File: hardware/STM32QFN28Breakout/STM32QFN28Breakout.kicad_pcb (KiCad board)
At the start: 2 copper layers, 22.7 x 34.6 mm, 21 parts, among them J5 Conn_01x11_Male, J6 Conn_01x11_Male, U1 STM32G031F4Px, U2 AP2112K-3.3, Y1 ECS-3225MVQ-160-BP-TR

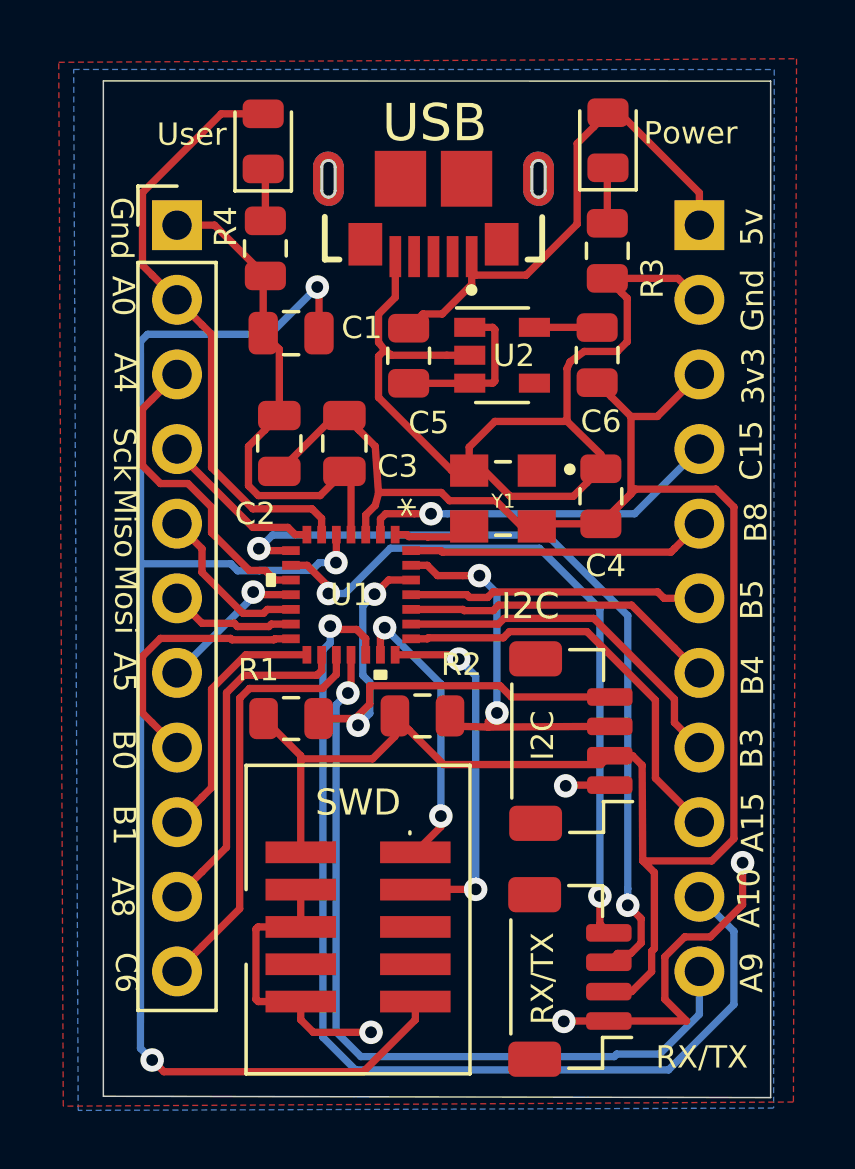
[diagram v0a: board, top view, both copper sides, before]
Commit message: fix and tweaks for STM32QFN28 breakout PCB
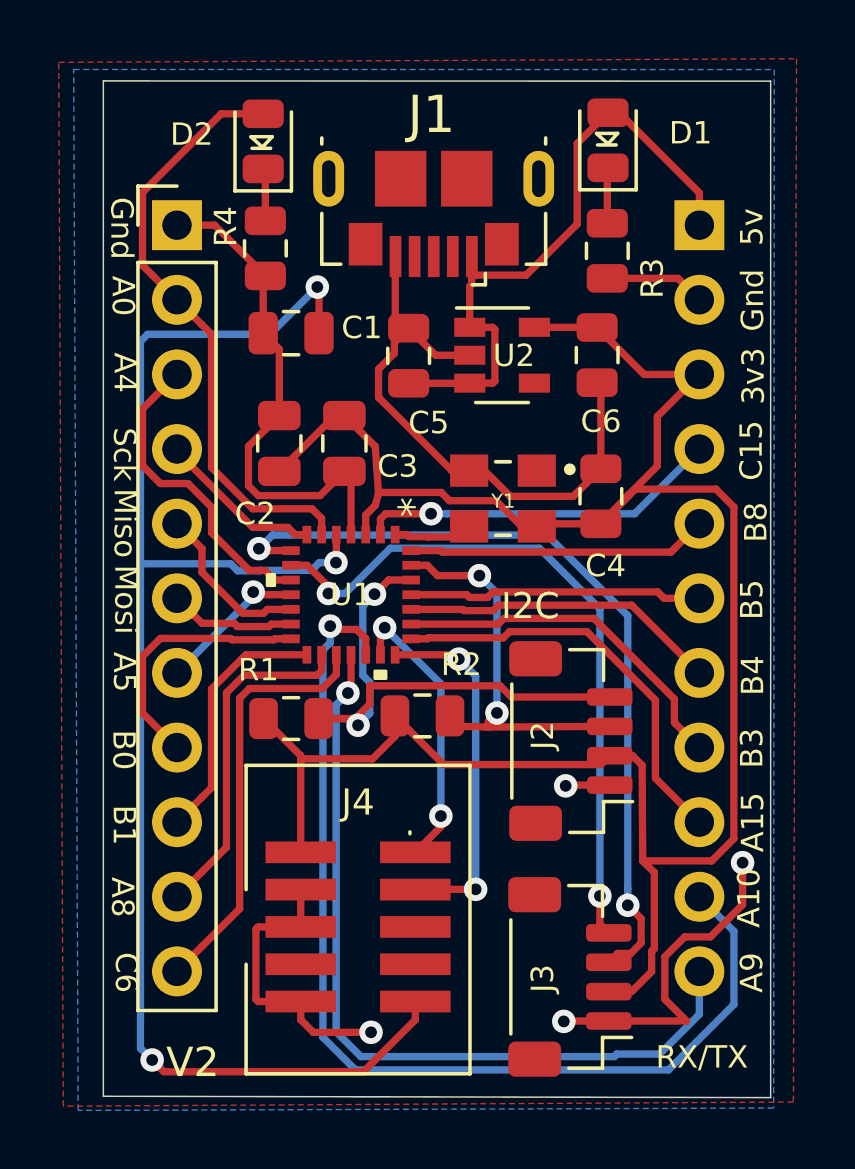
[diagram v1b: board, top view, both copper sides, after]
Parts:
- J1: renamed from USB; footprint Useful Modifications:GCT_USB3076-XX-X_REVC -> Useful Modifications:USB_Micro-B_GCT_USB3076-30-A
- moved J1 1.20 mm to (211.9, 80.9)
- renumbered Power to D1, User to D2, I2C to J2, RX/TX to J3, SWD to J4
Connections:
- C5 pad 1: Net-(C5-Pad1) -> +5V
- C5 pad 2: +5V -> GND
- C6 pad 1: +3V3 -> GND
- C6 pad 2: Net-(C6-Pad2) -> +3V3
- U2 pad 1: Net-(C5-Pad1) -> +5V
- U2 pad 3: Net-(C5-Pad1) -> +5V
- U2 pad 5: Net-(C6-Pad2) -> +3V3
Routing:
- net GND: track 74.8 -> 64.1 mm
- net Net-(C5-Pad1): track 5.60 -> 0.00 mm
- net +5V: track 18.1 -> 22.5 mm
- net +3V3: track 72.0 -> 76.2 mm
- net Net-(C6-Pad2): track 2.14 -> 0.00 mm
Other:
- board text added: "STM32G031G8U6 Breakout V2"
- board text added: "V2"

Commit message: updates to STM32QFN28 breakout moving to 0603 components
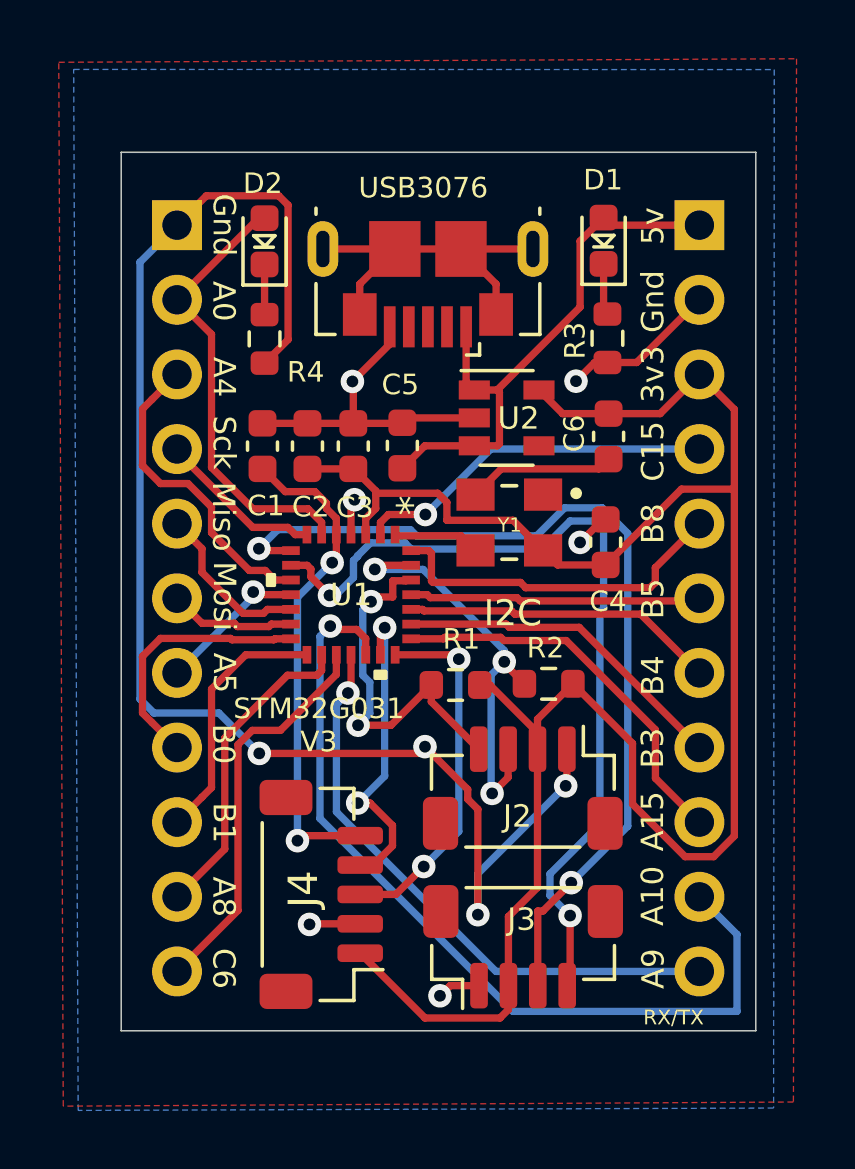
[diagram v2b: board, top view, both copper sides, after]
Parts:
- C1, C2, C3, C4, C5, C6: footprint Capacitor_SMD:C_0805_2012Metric -> Capacitor_SMD:C_0603_1608Metric
- D1, D2: footprint LED_SMD:LED_0805_2012Metric -> LED_SMD:LED_0603_1608Metric
- J1: value USB3076-XX-X_REVC -> USB3076
- J4: value Conn_ARM_JTAG_SWD_10 -> Conn_01x05_Male; footprint Useful Modifications:JTAG_SWD_SMD -> Connector_JST:JST_SH_BM05B-SRSS-TB_1x05-1MP_P1.00mm_Vertical
- R1, R2, R3, R4: footprint Resistor_SMD:R_0805_2012Metric -> Resistor_SMD:R_0603_1608Metric
- moved R1 5.71 mm to (212.7, 96.9), turned to 0 degrees
- moved R2 4.43 mm to (215.8, 96.9), turned to 0 degrees
- moved C1 3.97 mm to (206.1, 88.8), turned to 90 degrees
- moved D1 3.42 mm to (217.7, 81.8)
- moved D2 3.40 mm to (206.2, 81.8)
- moved R4 3.08 mm to (206.2, 85.2)
- moved C5 3.06 mm to (210.9, 88.8)
- moved R3 2.98 mm to (217.8, 85.1)
- moved C6 2.80 mm to (217.9, 88.5)
- moved J1 2.40 mm to (211.7, 83.3)
- moved J2 2.29 mm to (215.0, 100.4), turned to 180 degrees
- moved U2 2.14 mm to (214.4, 87.8)
- moved J3 1.90 mm to (215.0, 105.8), turned to 0 degrees
- moved J4 1.67 mm to (208.1, 104.1), turned to 90 degrees
- moved C4 1.57 mm to (217.8, 92.1)
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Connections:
- J1 pad 2: Net-(J1-Pad2) -> unconnected-(J1-Pad2)
- J1 pad 3: Net-(J1-Pad3) -> unconnected-(J1-Pad3)
- J1 pad 4: Net-(J1-Pad4) -> unconnected-(J1-Pad4)
- J1 pad 6: Net-(J1-Pad10) -> unconnected-(J1-Pad10)
- J4 pad 2: SWDIO -> GND
- J4 pad 3: GND -> SWCLK
- J4 pad 4: SWCLK -> SWDIO
- J4 pad 5: GND -> /RESET
- U2 pad 4: Net-(U2-Pad4) -> unconnected-(U2-Pad4)
- Y1 pad 1: Net-(Y1-Pad1) -> unconnected-(Y1-Pad1)
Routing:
- net /RESET: track 51.3 -> 17.0 mm, vias 3 -> 2
- net GND: track 64.1 -> 77.7 mm, vias 4 -> 10
- net unconnected-(J1-Pad10): track 0.00 -> 12.6 mm
- net PA9: track 27.8 -> 20.2 mm
- net SCL: track 18.7 -> 12.5 mm
- net RX: track 23.7 -> 29.5 mm
- net PA10: track 35.6 -> 30.0 mm
- net PA0: track 20.6 -> 15.3 mm
- net +3V3: track 76.2 -> 72.2 mm
- net TX: track 27.7 -> 31.6 mm
- net +5V: track 22.5 -> 19.3 mm
- net PB8: track 10.2 -> 12.1 mm
- net SWDIO: track 9.78 -> 10.9 mm
- net SDA: track 13.6 -> 14.7 mm, vias 2 -> 3
- net PC6: track 14.5 -> 13.6 mm
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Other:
- board size 22.7 x 34.6 mm -> 21.6 x 29.9 mm
- net class Default removed
- board text added: "STM32G031 V3"
- board text added: "STM32G031G8U6 Breakout V3"
- board text added: "USB3076"
- board text removed: "STM32G031G8U6 Breakout V2"
- board text removed: "V2"
